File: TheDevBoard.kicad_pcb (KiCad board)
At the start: 2 copper layers, 6 parts, among them J1 USB_C_Receptacle_USB2.0_16P, J2 USB_C_Receptacle_USB2.0_16P, U1 RP2350A, U2 ESP32-S3-MINI-1

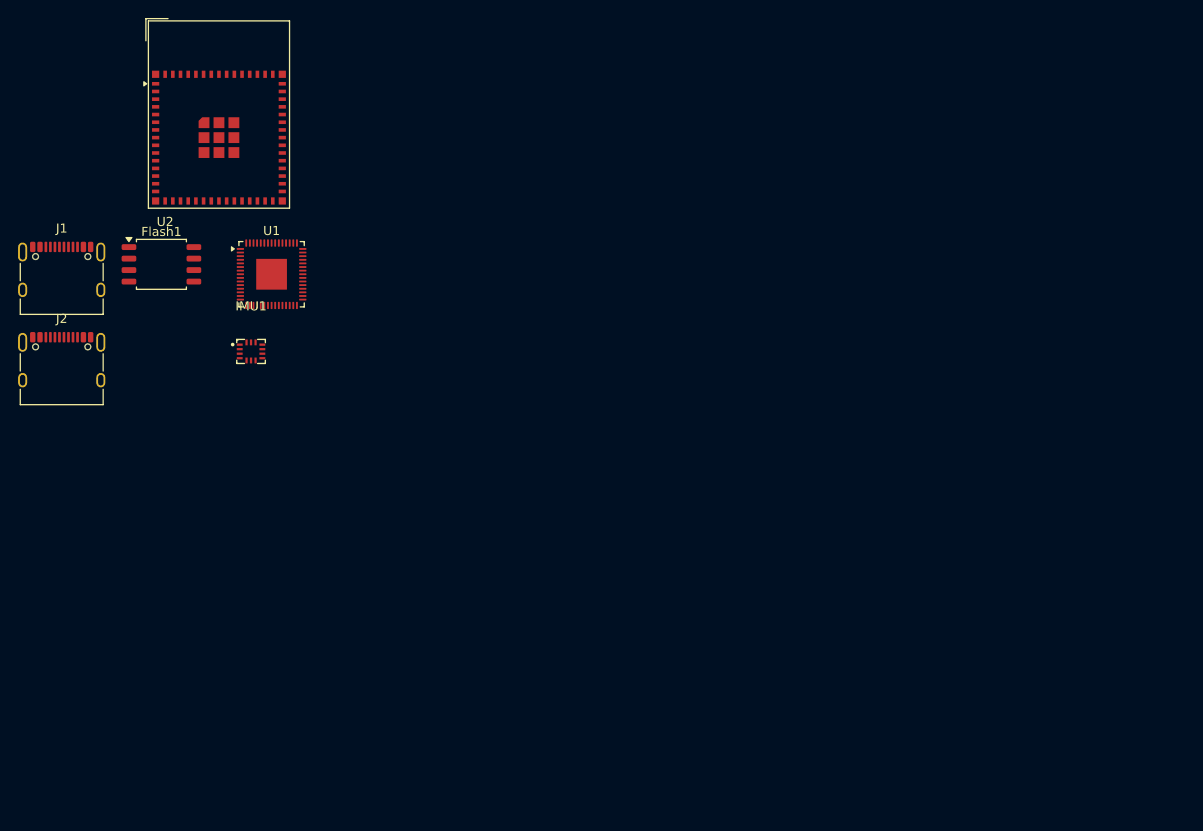
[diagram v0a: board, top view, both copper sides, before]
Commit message: added some lcsc part numbers
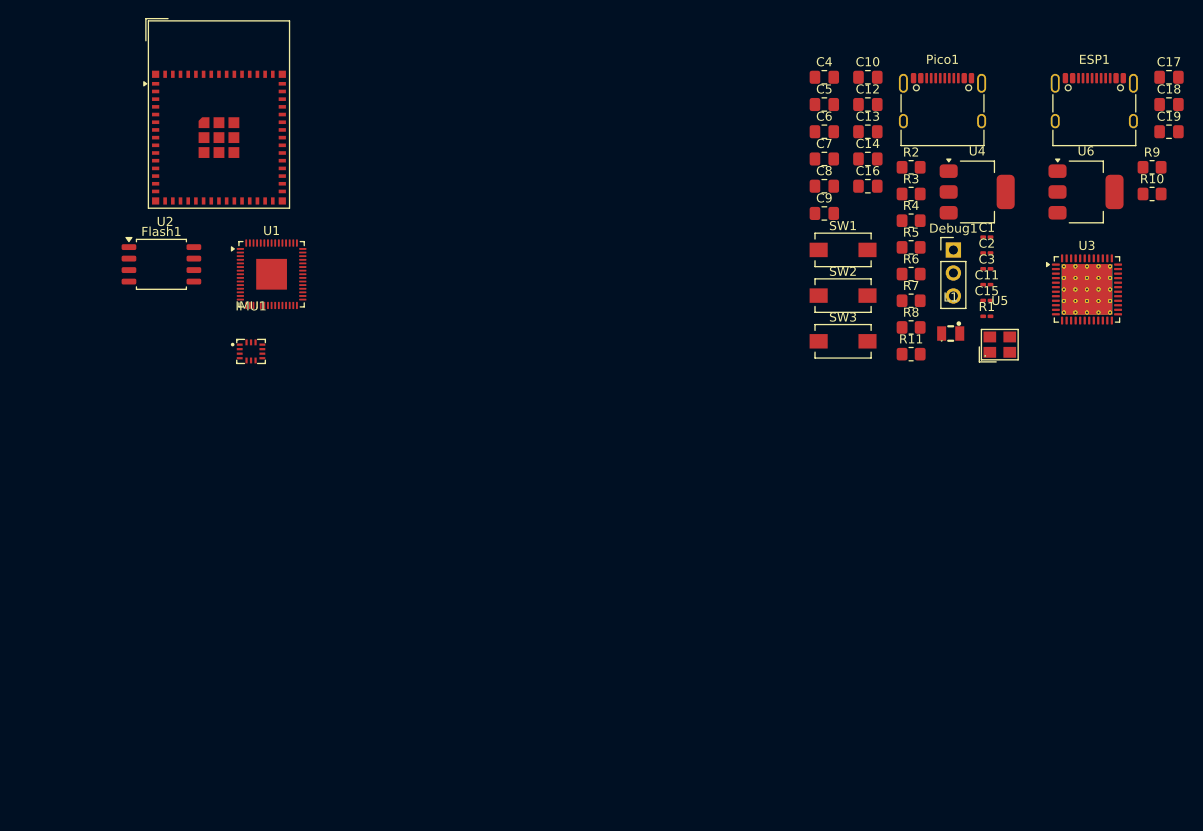
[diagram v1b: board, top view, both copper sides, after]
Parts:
- removed J1, J2: USB_C_Receptacle_USB2.0_16P, Connector_USB:USB_C_Receptacle_XKB_U262-16XN-4BVC11
- added C1: 4.7u, Capacitor_SMD:C_0201_0603Metric_Pad0.64x0.40mm_HandSolder, F.Cu at (220.9, 99.2)
- added C10: 15p, Capacitor_SMD:C_0805_2012Metric_Pad1.18x1.45mm_HandSolder, F.Cu at (207.7, 81.5)
- added C11: 4.7u, Capacitor_SMD:C_0201_0603Metric_Pad0.64x0.40mm_HandSolder, F.Cu at (220.9, 104.4)
- added C12: 47u, Capacitor_SMD:C_0805_2012Metric_Pad1.18x1.45mm_HandSolder, F.Cu at (207.7, 84.5)
- added C13: 100n, Capacitor_SMD:C_0805_2012Metric_Pad1.18x1.45mm_HandSolder, F.Cu at (207.7, 87.5)
- added C14: 100n, Capacitor_SMD:C_0805_2012Metric_Pad1.18x1.45mm_HandSolder, F.Cu at (207.7, 90.5)
- added C15: 4.7u, Capacitor_SMD:C_0201_0603Metric_Pad0.64x0.40mm_HandSolder, F.Cu at (220.9, 106.2)
- added C16: 100n, Capacitor_SMD:C_0805_2012Metric_Pad1.18x1.45mm_HandSolder, F.Cu at (207.7, 93.5)
- added C17: 47u, Capacitor_SMD:C_0805_2012Metric_Pad1.18x1.45mm_HandSolder, F.Cu at (241.0, 81.5)
- added C18: 47u, Capacitor_SMD:C_0805_2012Metric_Pad1.18x1.45mm_HandSolder, F.Cu at (241.0, 84.5)
- added C19: 100n, Capacitor_SMD:C_0805_2012Metric_Pad1.18x1.45mm_HandSolder, F.Cu at (241.0, 87.5)
- added C2: 4.7u, Capacitor_SMD:C_0201_0603Metric_Pad0.64x0.40mm_HandSolder, F.Cu at (220.9, 100.9)
- added C3: 4.7u, Capacitor_SMD:C_0201_0603Metric_Pad0.64x0.40mm_HandSolder, F.Cu at (220.9, 102.7)
- added C4: 47u, Capacitor_SMD:C_0805_2012Metric_Pad1.18x1.45mm_HandSolder, F.Cu at (202.9, 81.5)
- added C5: 47u, Capacitor_SMD:C_0805_2012Metric_Pad1.18x1.45mm_HandSolder, F.Cu at (202.9, 84.5)
- added C6: 100n, Capacitor_SMD:C_0805_2012Metric_Pad1.18x1.45mm_HandSolder, F.Cu at (202.9, 87.5)
- added C7: 100n, Capacitor_SMD:C_0805_2012Metric_Pad1.18x1.45mm_HandSolder, F.Cu at (202.9, 90.5)
- added C8: 100n, Capacitor_SMD:C_0805_2012Metric_Pad1.18x1.45mm_HandSolder, F.Cu at (202.9, 93.5)
- added C9: 15p, Capacitor_SMD:C_0805_2012Metric_Pad1.18x1.45mm_HandSolder, F.Cu at (202.9, 96.6)
- added Debug1: Conn_01x03_Pin, Connector_PinHeader_2.54mm:PinHeader_1x03_P2.54mm_Vertical, F.Cu at (217.2, 100.6)
- added ESP1: USB_C_Receptacle_USB2.0_16P, Connector_USB:USB_C_Receptacle_XKB_U262-16XN-4BVC11, F.Cu at (232.7, 85.3)
- added L1: AOTA-B201610S3R3-101-T, EasyEDA:IND-SMD_L2.0-W1.6_AOTA-B201610S3R3-101-T, F.Cu at (216.9, 109.8)
- added Pico1: USB_C_Receptacle_USB2.0_16P, Connector_USB:USB_C_Receptacle_XKB_U262-16XN-4BVC11, F.Cu at (216.0, 85.3)
- added R1: 33, Resistor_SMD:R_0201_0603Metric_Pad0.64x0.40mm_HandSolder, F.Cu at (220.9, 107.9)
- added R10: 5.1k, Resistor_SMD:R_0805_2012Metric_Pad1.20x1.40mm_HandSolder, F.Cu at (239.1, 94.4)
- added R11: 1k, Resistor_SMD:R_0805_2012Metric_Pad1.20x1.40mm_HandSolder, F.Cu at (212.5, 112.1)
- added R2: 5.1k, Resistor_SMD:R_0805_2012Metric_Pad1.20x1.40mm_HandSolder, F.Cu at (212.5, 91.5)
- added R3: 5.1k, Resistor_SMD:R_0805_2012Metric_Pad1.20x1.40mm_HandSolder, F.Cu at (212.5, 94.4)
- added R4: 1k, Resistor_SMD:R_0805_2012Metric_Pad1.20x1.40mm_HandSolder, F.Cu at (212.5, 97.4)
- added R5: 1k, Resistor_SMD:R_0805_2012Metric_Pad1.20x1.40mm_HandSolder, F.Cu at (212.5, 100.3)
- added R6: 1k, Resistor_SMD:R_0805_2012Metric_Pad1.20x1.40mm_HandSolder, F.Cu at (212.5, 103.3)
- added R7: 27, Resistor_SMD:R_0805_2012Metric_Pad1.20x1.40mm_HandSolder, F.Cu at (212.5, 106.2)
- added R8: 27, Resistor_SMD:R_0805_2012Metric_Pad1.20x1.40mm_HandSolder, F.Cu at (212.5, 109.2)
- added R9: 5.1k, Resistor_SMD:R_0805_2012Metric_Pad1.20x1.40mm_HandSolder, F.Cu at (239.1, 91.5)
- added SW1: SW_Push, Button_Switch_SMD:SW_SPST_EVQPE1, F.Cu at (205.0, 100.6)
- added SW2: SW_Push, Button_Switch_SMD:SW_SPST_EVQPE1, F.Cu at (205.0, 105.6)
- added SW3: SW_Push, Button_Switch_SMD:SW_SPST_EVQPE1, F.Cu at (205.0, 110.7)
- added U3: ICE40UP5K-SG48ITR, Package_DFN_QFN:QFN-48-1EP_7x7mm_P0.5mm_EP5.6x5.6mm_ThermalVias, F.Cu at (231.9, 105.0)
- added U4: AMS1117-3.3, Package_TO_SOT_SMD:SOT-223-3_TabPin2, F.Cu at (219.8, 94.2)
- added U5: ABM8-272-T3_C20625731, EasyEDA:CRYSTAL-SMD_4P-L3.2-W2.5-BL, F.Cu at (222.3, 111.1)
- added U6: AMS1117-3.3, Package_TO_SOT_SMD:SOT-223-3_TabPin2, F.Cu at (231.8, 94.2)
- Flash1: value W25Q32JVSS -> W25Q128JVS
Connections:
- Flash1 pad 1: unconnected-(Flash1-~{CS}-Pad1) -> /RP2350/BOOT
- Flash1 pad 2: unconnected-(Flash1-DO/IO_{1}-Pad2) -> Net-(Flash1-DO/IO_{1})
- Flash1 pad 3: unconnected-(Flash1-~{WP}/IO_{2}-Pad3) -> Net-(Flash1-~{WP}/IO_{2})
- Flash1 pad 4: unconnected-(Flash1-GND-Pad4) -> GND
- Flash1 pad 5: unconnected-(Flash1-DI/IO_{0}-Pad5) -> Net-(Flash1-DI/IO_{0})
- Flash1 pad 6: unconnected-(Flash1-CLK-Pad6) -> Net-(Flash1-CLK)
- Flash1 pad 7: unconnected-(Flash1-~{HOLD}/~{RESET}/IO_{3}-Pad7) -> Net-(Flash1-~{HOLD}/~{RESET}/IO_{3})
- Flash1 pad 8: unconnected-(Flash1-VCC-Pad8) -> +3V3
- U1 pad 1: Net-(U1-IOVDD-Pad1) -> +3V3
- U1 pad 11: Net-(U1-IOVDD-Pad1) -> +3V3
- U1 pad 20: Net-(U1-IOVDD-Pad1) -> +3V3
- U1 pad 21: unconnected-(U1-XIN-Pad21) -> /RP2350/XIN
- U1 pad 22: unconnected-(U1-XOUT-Pad22) -> Net-(U1-XOUT)
- U1 pad 23: Net-(U1-DVDD-Pad23) -> +3V3
- U1 pad 24: unconnected-(U1-SWCLK-Pad24) -> /RP2350/SWCLK
- U1 pad 25: unconnected-(U1-SWDIO-Pad25) -> /RP2350/SWDIO
- U1 pad 26: unconnected-(U1-RUN-Pad26) -> /RP2350/RUN
- U1 pad 30: Net-(U1-IOVDD-Pad1) -> +3V3
- U1 pad 38: Net-(U1-IOVDD-Pad1) -> +3V3
- U1 pad 39: Net-(U1-DVDD-Pad23) -> +3V3
- U1 pad 44: unconnected-(U1-ADC_AVDD-Pad44) -> +3V3
- U1 pad 45: Net-(U1-IOVDD-Pad1) -> +3V3
- U1 pad 46: unconnected-(U1-VREG_AVDD-Pad46) -> Net-(U1-VREG_AVDD)
- U1 pad 47: unconnected-(U1-VREG_PGND-Pad47) -> GND
- U1 pad 48: unconnected-(U1-VREG_LX-Pad48) -> Net-(U1-VREG_LX)
- U1 pad 49: unconnected-(U1-VREG_VIN-Pad49) -> +3V3
- U1 pad 50: unconnected-(U1-VREG_FB-Pad50) -> +1V1
- U1 pad 51: unconnected-(U1-USB_DM-Pad51) -> Net-(U1-USB_DM)
- U1 pad 52: unconnected-(U1-USB_DP-Pad52) -> Net-(U1-USB_DP)
- U1 pad 53: unconnected-(U1-USB_OTP_VDD-Pad53) -> +3V3
- U1 pad 54: unconnected-(U1-QSPI_IOVDD-Pad54) -> +3V3
- U1 pad 55: unconnected-(U1-QSPI_SD3-Pad55) -> Net-(Flash1-~{HOLD}/~{RESET}/IO_{3})
- U1 pad 56: unconnected-(U1-QSPI_SCLK-Pad56) -> Net-(Flash1-CLK)
- U1 pad 57: unconnected-(U1-QSPI_SD0-Pad57) -> Net-(Flash1-DI/IO_{0})
- U1 pad 58: unconnected-(U1-QSPI_SD2-Pad58) -> Net-(Flash1-~{WP}/IO_{2})
- U1 pad 59: unconnected-(U1-QSPI_SD1-Pad59) -> Net-(Flash1-DO/IO_{1})
- U1 pad 6: Net-(U1-DVDD-Pad23) -> +3V3
- U1 pad 60: unconnected-(U1-~{QSPI_SS}-Pad60) -> /RP2350/BOOT
- U1 pad 61: unconnected-(U1-GND-Pad61) -> GND

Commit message: created esp32 s3 mini connection to rp2350 added SD card Routed them together
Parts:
- removed C18: 47u, Capacitor_SMD:C_0805_2012Metric_Pad1.18x1.45mm_HandSolder
- removed C19: 100n, Capacitor_SMD:C_0805_2012Metric_Pad1.18x1.45mm_HandSolder
- removed U6: AMS1117-3.3, Package_TO_SOT_SMD:SOT-223-3_TabPin2
- added C20: 100n, Capacitor_SMD:C_0805_2012Metric_Pad1.18x1.45mm_HandSolder, F.Cu at (129.9, 155.7)
- added C21: 47u, Capacitor_SMD:C_0805_2012Metric_Pad1.18x1.45mm_HandSolder, F.Cu at (129.9, 158.7)
- added C22: 47u, Capacitor_SMD:C_0805_2012Metric_Pad1.18x1.45mm_HandSolder, F.Cu at (129.9, 161.7)
- added C23: 100n, Capacitor_SMD:C_0805_2012Metric_Pad1.18x1.45mm_HandSolder, F.Cu at (147.6, 124.0)
- added C24: 47u, Capacitor_SMD:C_0805_2012Metric_Pad1.18x1.45mm_HandSolder, F.Cu at (147.6, 127.0)
- added C25: 100n, Capacitor_SMD:C_0805_2012Metric_Pad1.18x1.45mm_HandSolder, F.Cu at (147.6, 130.0)
- added C26: 100n, Capacitor_SMD:C_0805_2012Metric_Pad1.18x1.45mm_HandSolder, F.Cu at (147.6, 133.0)
- added C27: 47u, Capacitor_SMD:C_0805_2012Metric_Pad1.18x1.45mm_HandSolder, F.Cu at (147.6, 136.0)
- added Card1: TF PUSH, EasyEDA:TF-SMD_TF-PUSH, F.Cu at (136.3, 129.1)
- added D1: D, Diode_SMD:D_0805_2012Metric, F.Cu at (145.4, 151.2)
- added D2: D, Diode_SMD:D_0805_2012Metric, F.Cu at (129.7, 140.9)
- added D3: D, Diode_SMD:D_0805_2012Metric, F.Cu at (134.6, 155.7)
- added D4: D, Diode_SMD:D_0805_2012Metric, F.Cu at (134.6, 158.8)
- added F1: JK-SMD0805-020-30V, EasyEDA:F0805, F.Cu at (137.1, 151.2)
- added L2: FTC252010S4R7MBCA, EasyEDA:IND-SMD_L2.5-W2.0-VLS252012CX-150M, F.Cu at (138.6, 158.8)
- added Power1: LED, LED_SMD:LED_0805_2012Metric, F.Cu at (134.6, 161.8)
- added R12: 1k, Resistor_SMD:R_0805_2012Metric, F.Cu at (139.0, 155.7)
- added R13: 10k, Resistor_SMD:R_0805_2012Metric_Pad1.20x1.40mm_HandSolder, F.Cu at (152.4, 124.0)
- added R15: 10k, Resistor_SMD:R_0805_2012Metric_Pad1.20x1.40mm_HandSolder, F.Cu at (152.4, 126.9)
- added R16: 10k, Resistor_SMD:R_0805_2012Metric_Pad1.20x1.40mm_HandSolder, F.Cu at (152.4, 129.9)
- added R17: 10k, Resistor_SMD:R_0805_2012Metric_Pad1.20x1.40mm_HandSolder, F.Cu at (152.4, 132.8)
- added R18: 10k, Resistor_SMD:R_0805_2012Metric_Pad1.20x1.40mm_HandSolder, F.Cu at (152.4, 135.8)
- added SW4: SW_Push, Button_Switch_SMD:SW_SPST_EVQPE1, F.Cu at (149.7, 140.1)
- added SW5: SW_Push, Button_Switch_SMD:SW_SPST_EVQPE1, F.Cu at (149.7, 145.1)
- added U7: AP63205WU, Package_TO_SOT_SMD:TSOT-23-6_HandSoldering, F.Cu at (131.0, 152.0)
- C17: value 47u -> 100n
- moved C1 39.2 mm to (181.7, 101.8)
- moved C10 39.2 mm to (168.6, 84.2)
- moved C11 39.2 mm to (181.7, 107.1)
- moved C12 39.2 mm to (168.6, 87.2)
- moved C13 39.2 mm to (168.6, 90.2)
- moved C14 39.2 mm to (168.6, 93.2)
- moved C15 39.2 mm to (181.7, 108.8)
- moved C16 39.2 mm to (168.6, 96.2)
- moved C17 39.2 mm to (201.8, 84.2)
- moved C2 39.2 mm to (181.7, 103.6)
- moved C3 39.2 mm to (181.7, 105.3)
- moved C4 39.2 mm to (163.8, 84.2)
- moved C5 39.2 mm to (163.8, 87.2)
- moved C6 39.2 mm to (163.8, 90.2)
- moved C7 39.2 mm to (163.8, 93.2)
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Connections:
- C17 pad 1: +5V -> /ESP32-S3-Mini-WIFI/EN
- ESP1 pad A4: +5V -> Net-(D2-A)
- ESP1 pad A9: +5V -> Net-(D2-A)
- ESP1 pad B4: +5V -> Net-(D2-A)
- ESP1 pad B9: +5V -> Net-(D2-A)
- Pico1 pad A4: +5V -> Net-(D1-A)
- Pico1 pad A9: +5V -> Net-(D1-A)
- Pico1 pad B4: +5V -> Net-(D1-A)
- Pico1 pad B9: +5V -> Net-(D1-A)
- U1 pad 2: unconnected-(U1-GPIO0-Pad2) -> /ESP32-S3-Mini-WIFI/UART_RX_ESP
- U1 pad 27: unconnected-(U1-GPIO16-Pad27) -> /ESP32-S3-Mini-WIFI/FSPIQ
- U1 pad 28: unconnected-(U1-GPIO17-Pad28) -> /ESP32-S3-Mini-WIFI/FSPICS0
- U1 pad 29: unconnected-(U1-GPIO18-Pad29) -> /ESP32-S3-Mini-WIFI/FSPICLK
- U1 pad 3: unconnected-(U1-GPIO1-Pad3) -> /ESP32-S3-Mini-WIFI/UART_TX_ESP
- U1 pad 31: unconnected-(U1-GPIO19-Pad31) -> /ESP32-S3-Mini-WIFI/FSPID
- U1 pad 32: unconnected-(U1-GPIO20-Pad32) -> /ESP32-S3-Mini-WIFI/Handshake
- U1 pad 33: unconnected-(U1-GPIO21-Pad33) -> /ESP32-S3-Mini-WIFI/DataReadyInt
- U2 pad 1: Net-(U2-GND-Pad1) -> GND
- U2 pad 10: unconnected-(U2-IO6-Pad10) -> /ESP32-S3-Mini-WIFI/SPI_CMD
- U2 pad 11: unconnected-(U2-IO7-Pad11) -> /ESP32-S3-Mini-WIFI/SPI_CS
- U2 pad 14: unconnected-(U2-IO10-Pad14) -> /ESP32-S3-Mini-WIFI/FSPICS0
- U2 pad 15: unconnected-(U2-IO11-Pad15) -> /ESP32-S3-Mini-WIFI/FSPID
- U2 pad 16: unconnected-(U2-IO12-Pad16) -> /ESP32-S3-Mini-WIFI/FSPICLK
- U2 pad 17: unconnected-(U2-IO13-Pad17) -> /ESP32-S3-Mini-WIFI/FSPIQ
- U2 pad 18: unconnected-(U2-IO14-Pad18) -> /ESP32-S3-Mini-WIFI/Handshake
- U2 pad 2: Net-(U2-GND-Pad1) -> GND
- U2 pad 23: unconnected-(U2-USB_D--Pad23) -> /ESP32-S3-Mini-WIFI/D-
- U2 pad 24: unconnected-(U2-USB_D+-Pad24) -> /ESP32-S3-Mini-WIFI/D+
- U2 pad 25: unconnected-(U2-IO21-Pad25) -> /ESP32-S3-Mini-WIFI/DataReadyInt
- U2 pad 3: unconnected-(U2-3V3-Pad3) -> +3V3
- U2 pad 39: unconnected-(U2-TXD0-Pad39) -> /ESP32-S3-Mini-WIFI/UART_TX_ESP
- U2 pad 4: unconnected-(U2-IO0-Pad4) -> /ESP32-S3-Mini-WIFI/BOOT
- U2 pad 40: unconnected-(U2-RXD0-Pad40) -> /ESP32-S3-Mini-WIFI/UART_RX_ESP
- U2 pad 42: Net-(U2-GND-Pad1) -> GND
- U2 pad 43: Net-(U2-GND-Pad1) -> GND
- U2 pad 45: unconnected-(U2-EN-Pad45) -> /ESP32-S3-Mini-WIFI/EN
- U2 pad 46: Net-(U2-GND-Pad1) -> GND
- U2 pad 47: Net-(U2-GND-Pad1) -> GND
- U2 pad 48: Net-(U2-GND-Pad1) -> GND
- U2 pad 49: Net-(U2-GND-Pad1) -> GND
- U2 pad 50: Net-(U2-GND-Pad1) -> GND
- U2 pad 51: Net-(U2-GND-Pad1) -> GND
- U2 pad 52: Net-(U2-GND-Pad1) -> GND
- U2 pad 53: Net-(U2-GND-Pad1) -> GND
- U2 pad 54: Net-(U2-GND-Pad1) -> GND
- U2 pad 55: Net-(U2-GND-Pad1) -> GND
- U2 pad 56: Net-(U2-GND-Pad1) -> GND
- U2 pad 57: Net-(U2-GND-Pad1) -> GND
- U2 pad 58: Net-(U2-GND-Pad1) -> GND
- U2 pad 59: Net-(U2-GND-Pad1) -> GND
- U2 pad 60: Net-(U2-GND-Pad1) -> GND
- U2 pad 61: Net-(U2-GND-Pad1) -> GND
- U2 pad 62: Net-(U2-GND-Pad1) -> GND
- U2 pad 63: Net-(U2-GND-Pad1) -> GND
- U2 pad 64: Net-(U2-GND-Pad1) -> GND
- U2 pad 65: Net-(U2-GND-Pad1) -> GND
- U2 pad 8: unconnected-(U2-IO4-Pad8) -> /ESP32-S3-Mini-WIFI/SPI_CLK
- U2 pad 9: unconnected-(U2-IO5-Pad9) -> /ESP32-S3-Mini-WIFI/SPI_D0
